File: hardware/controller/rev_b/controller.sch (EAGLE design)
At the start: 96 parts, among them J1 MODULE_CONTROLLER, J14 SOLDERJUMPERTRACE, J15 SOLDERJUMPERTRACE, J2 DM3AT-SF-PEJM5, J3 U.FL-R-SMT, J4 MICRO_USB_B_HIROSE_ZX62-B-5PA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, J5 MICRO_USB_B_HIROSE_ZX62-B-5PA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, J6 TC2030-JLINK-L, J7 TC2030-JLINK-L, J8 JUMPER-3PTH, Q1 MOSFET-NCHANNELSMD, Q2 NX3008PBK, SW1 PTS810SJ, SW2 SIP3240X, U1 SAM4LC8AA, U2 SAM4LC8AA, U3 RXM-GPS-RM-T, U4 FM25CLXXB-DG, U5 TS3USB30E, U6 FTDI234XD, U7 TXS0108EVQFN20, X1 16MHz, X2 16MHz

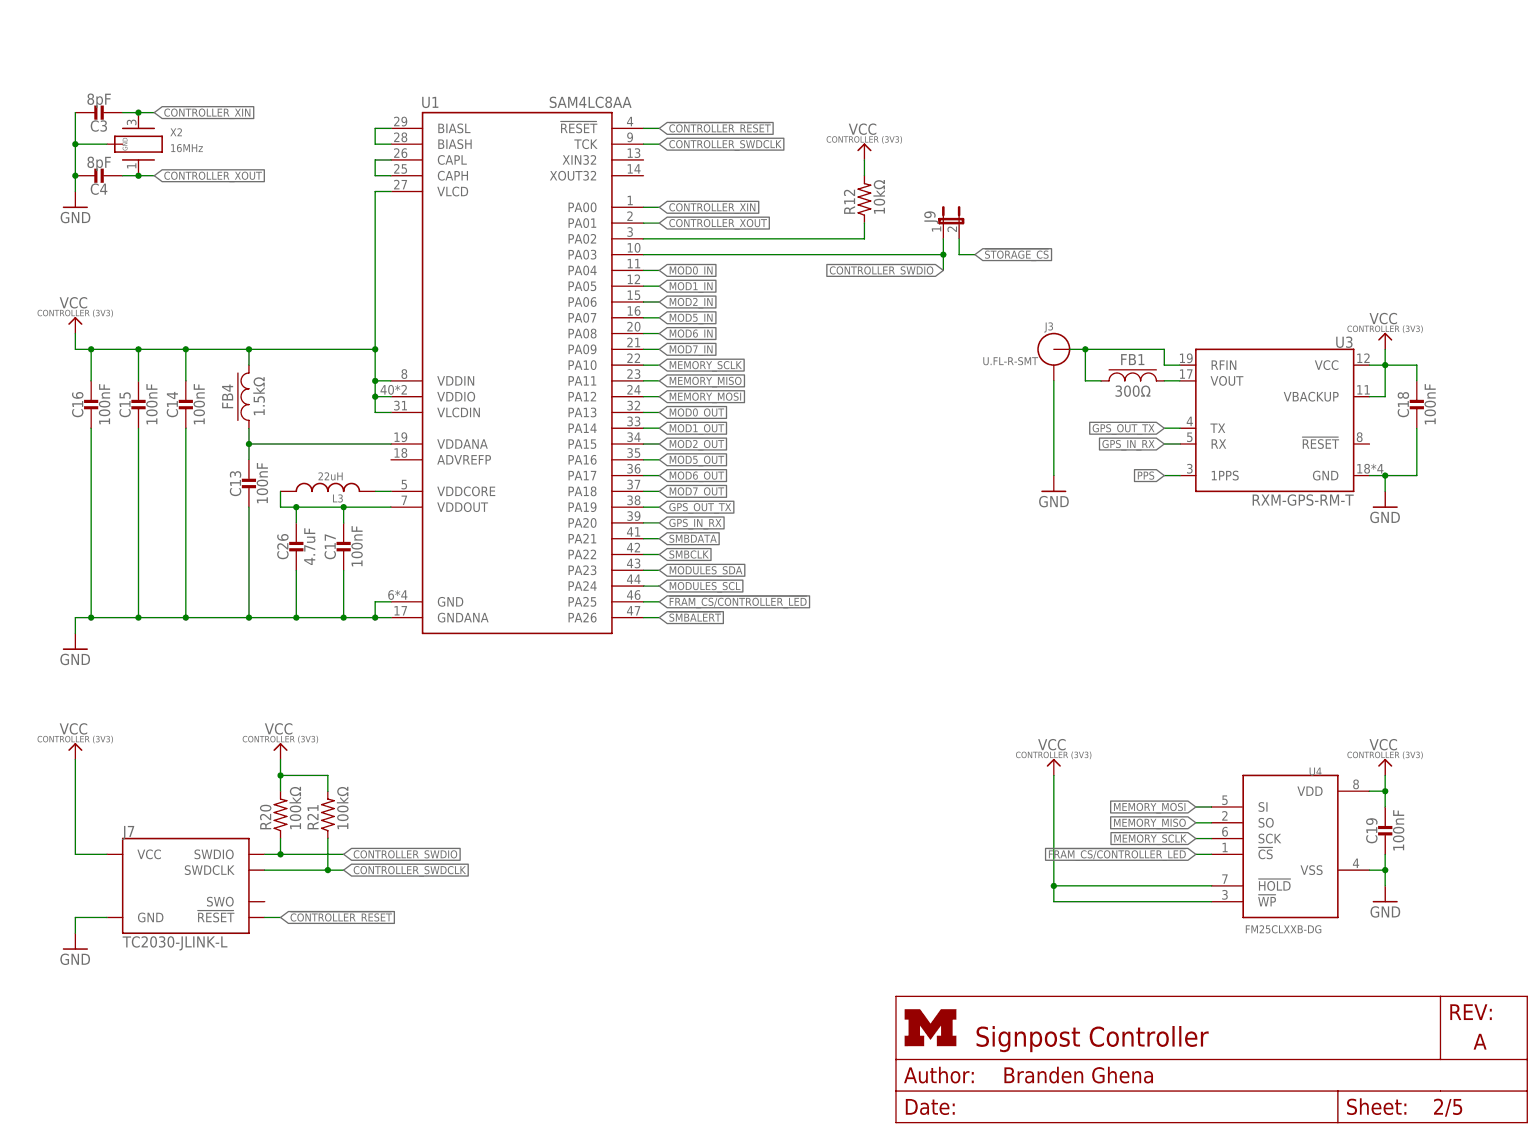
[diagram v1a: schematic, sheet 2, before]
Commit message: Controller rev B, schematic is complete
Updates:
 * Power gates for SD Card and GPS (that should work)
 * Re-do USB OTG circuitry based on [Intel Edison Gateway v3](https://github.com/lab11/IntelEdisonGateway/tree/master/hardware/v3)
 * Add debug headers
 * Upgrade to 64-pin SAM4Ls
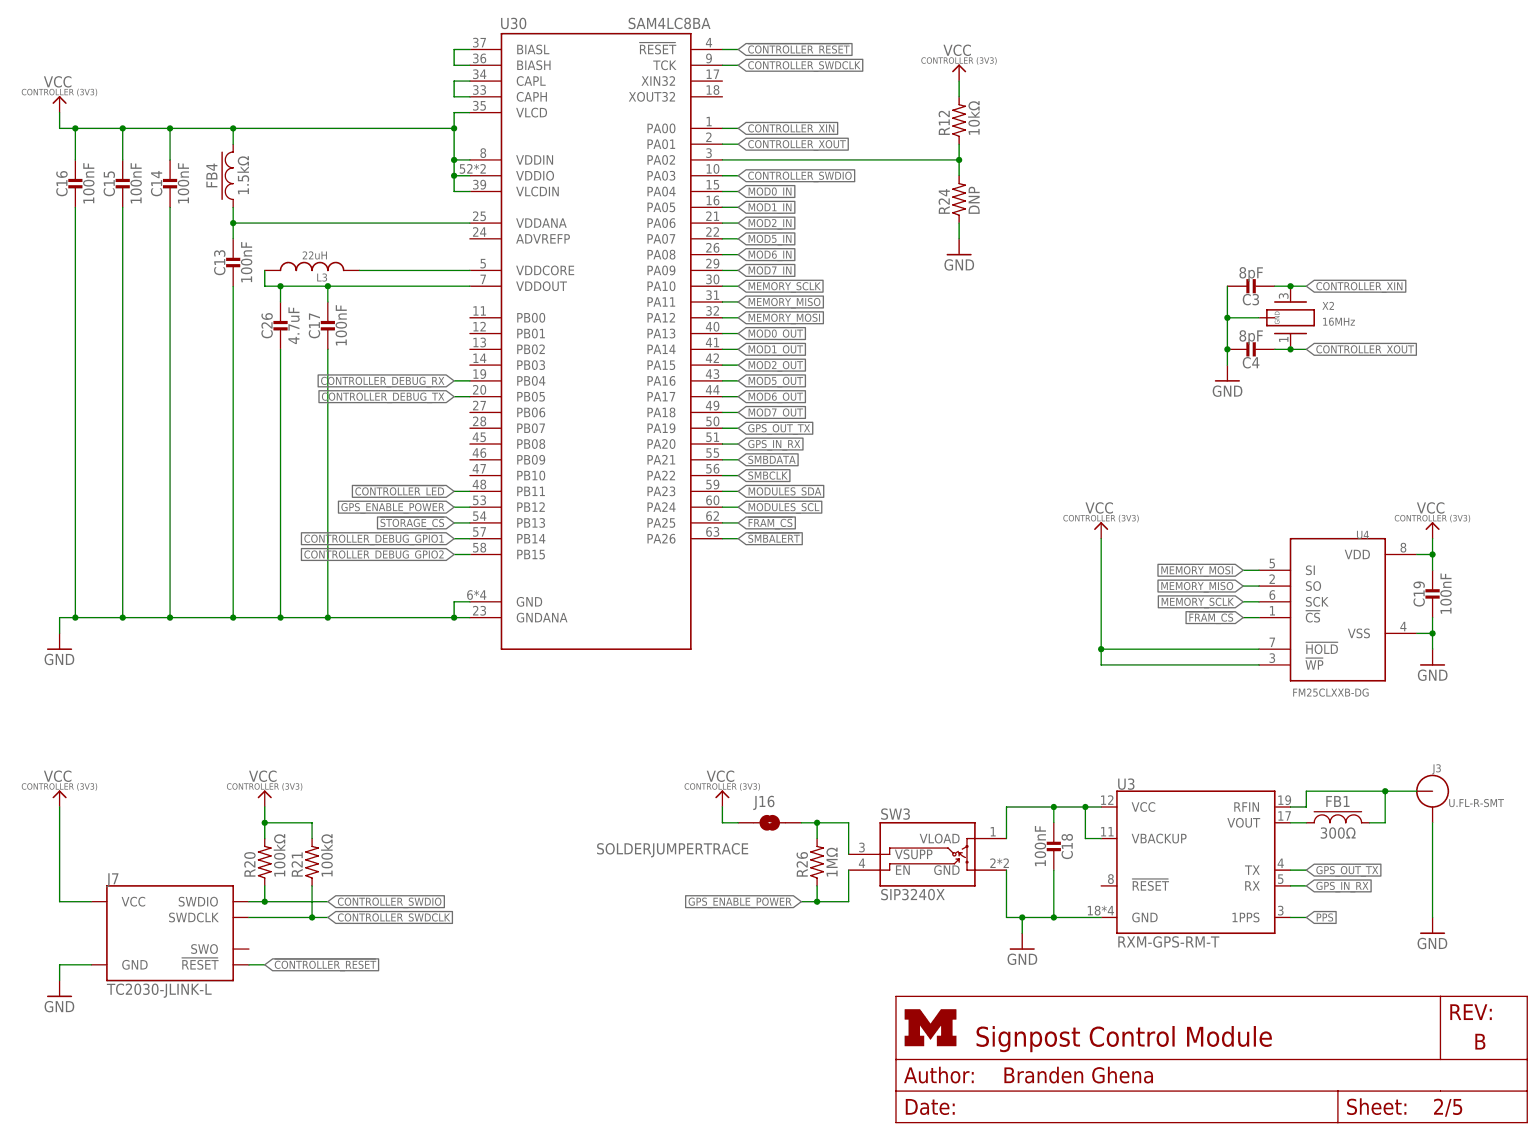
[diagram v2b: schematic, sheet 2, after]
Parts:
- removed J4: MICRO_USB_B_HIROSE_ZX62-B-5PA(11), connector:MICRO_USB_B_HIROSE_ZX62-B-5PA(11)
- removed J8: JUMPER-3PTH, umich:JUMPER-3PTH
- removed J9: (no value), umich:JUMPER-2PTH
- removed Q2: NX3008PBK, fets:NX3008PBK
- removed U1, U2: SAM4LC8AA, chips:SAM4LC8AA
- added J16, J17: SOLDERJUMPERTRACE, SparkFun-Passives:SOLDERJUMPERTRACE
- added J18: MICRO_USB_B_HIROSE_ZX62R-B-5P, connector:MICRO_USB_B_HIROSE_ZX62R-B-5P
- added R26, R27: 1MΩ, passives:RESISTOR0402_RES
- added R28: DNP, passives:RESISTOR0402_RES
- added SW3, SW4: SIP3240X, signpost:SIP3240X
- added U29, U30: SAM4LC8BA, chips:SAM4LC8BA
- added U8: SN74LVC1G125DBVR, chips:SN74LVC1G125DBVR
- J5: value MICRO_USB_B_HIROSE_ZX62-B-5PA(11) -> MICRO_USB_B_HIROSE_ZX62R-B-5P; device connector:MICRO_USB_B_HIROSE_ZX62-B-5PA(11) -> connector:MICRO_USB_B_HIROSE_ZX62R-B-5P; DIGIKEY (none) -> H125274CT-ND
- Q1: value MOSFET-NCHANNELSMD -> DMN32D2LDF; device fets:MOSFET-NCHANNELSMD -> fets:DMN32D2LDF; DIGIKEY SI2312CDS-T1-GE3CT-ND -> (none)
- R13: value 10kΩ -> 100kΩ; DIGIKEY 1276-3431-1-ND -> 1276-3429-1-ND
- R23: value 332kΩ -> 100kΩ; DIGIKEY 1276-4245-1-ND -> 1276-3429-1-ND
- R24: value 665kΩ -> DNP; DIGIKEY 1276-4275-1-ND -> 1276-3431-1-ND
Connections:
- removed net !FRAM_CS/CONTROLLER_LED: J10.9, R10.2, U1.PA25, U4.!CS
- removed net N$16: J8.1, R23.1, R24.2
- removed net N$19: J1CONTROLLER.DBG_TX
- removed net N$20: J1CONTROLLER.DBG_RX
- removed net N$21: J1CONTROLLER.DBG_SWDIO
- removed net N$22: J1CONTROLLER.DBG_SWDCLK
- removed net N$23: J1CONTROLLER.DBG_!RESET
- removed net N$26: J1CONTROLLER.DBG_GPIO1
- removed net N$27: J1CONTROLLER.DBG_GPIO2
- removed net N$33: J1CONTROLLER.GND1
- removed net N$35: J1STORAGE_MASTER.GND1
- removed net N$36: J1STORAGE_MASTER.DBG_GPIO2
- removed net N$39: J1STORAGE_MASTER.DBG_GPIO1
- removed net N$40: J1STORAGE_MASTER.DBG_!RESET
- removed net N$41: J1STORAGE_MASTER.DBG_SWDCLK
- removed net N$42: J1STORAGE_MASTER.DBG_SWDIO
- removed net N$47: J1STORAGE_MASTER.DBG_RX
- removed net N$49: J1STORAGE_MASTER.DBG_TX
- removed net N$52: L3.2, U1.VDDCORE
- removed net SD_DISABLE: Q2.G, R13.2
- removed net SD_ENABLE: U2.PA21
- removed net USB_ATTACHED_3V3: J8.2, Q1.G, U5.S
- new net !CONTROLLER_LED: R10.2, U30.PB11
- new net !FRAM_CS: J10.9, U30.PA25, U4.!CS
- new net CONTROLLER_DEBUG_GPIO1: J1CONTROLLER.DBG_GPIO1, U30.PB14
- new net CONTROLLER_DEBUG_GPIO2: J1CONTROLLER.DBG_GPIO2, U30.PB15
- new net CONTROLLER_DEBUG_RX: J1CONTROLLER.DBG_RX, U30.PB04
- new net CONTROLLER_DEBUG_TX: J1CONTROLLER.DBG_TX, U30.PB05
- new net GPS_ENABLE_POWER: R26.1, SW3.EN, U30.PB12
- new net N$55: J16.2, R26.2, SW3.VSUPP
- new net N$56: C18.1, SW3.VLOAD, U3.VBACKUP, U3.VCC
- new net N$57: J17.2, R27.2, SW4.VSUPP
- new net N$58: C27.1, J2.VCC, R14.2, R15.2, R16.2, R22.2, SW4.VLOAD
- new net N$59: L3.2, U30.VDDCORE
- new net SD_ENABLE_POWER: R27.1, SW4.EN, U29.PA21
- new net STORAGE_DEBUG_GPIO1: J1STORAGE_MASTER.DBG_GPIO1, U29.PB04
- new net STORAGE_DEBUG_GPIO2: J1STORAGE_MASTER.DBG_GPIO2, U29.PB05
- new net STORAGE_DEBUG_RX: J1STORAGE_MASTER.DBG_RX, U29.PB09
- new net STORAGE_DEBUG_TX: J1STORAGE_MASTER.DBG_TX, U29.PB10
- net !CONTROLLER_RESET: now also J1CONTROLLER.DBG_!RESET, U30.!RESET; no longer U1.!RESET
- net !EDISON_PWRBTN: now also U29.PA05; no longer U2.PA05
- net !EDISON_SPI_CS: now also U29.PA22; no longer U2.PA22
- net !SD_CS: now also U29.PA13; no longer U2.PA13
- net !SMBALERT: now also U30.PA26; no longer U1.PA26
- net !STORAGE_CS: now also U29.PA09, U30.PB13; no longer J9.2, U2.PA09
- net !STORAGE_LED: now also U29.PA07; no longer U2.PA07
- net !STORAGE_RESET: now also J1STORAGE_MASTER.DBG_!RESET, U29.!RESET; no longer U2.!RESET
- net CONTROLLER_BUCK/LDO_N: now also R24.2, U30.PA02; no longer U1.PA02
- net CONTROLLER_SWDCLK: now also J1CONTROLLER.DBG_SWDCLK, U30.TCK; no longer U1.TCK
- net CONTROLLER_SWDIO: now also J1CONTROLLER.DBG_SWDIO, U30.PA03; no longer J9.1, U1.PA03
- net CONTROLLER_XIN: now also U30.PA00; no longer U1.PA00
- net CONTROLLER_XOUT: now also U30.PA01; no longer U1.PA01
- net D+: now also J18.D+; no longer J5.D+
- net D-: now also J18.D-; no longer J5.D-
- net EDISON_SPI_MISO: now also U29.PA20; no longer U2.PA20
- net EDISON_SPI_MOSI: now also U29.PA19; no longer U2.PA19
- net EDISON_SPI_SCLK: now also U29.PA18; no longer U2.PA18
- net GND: now also J18.GND, J1CONTROLLER.GND1, J1STORAGE_MASTER.GND1, R13.2, R28.1, SW3.GND, SW4.GND, U29.GND, U29.GNDANA, U30.GND, U30.GNDANA, U8.A, U8.GND; no longer J4.GND, R13.1, U1.GND, U1.GNDANA, U2.GND, U2.GNDANA
- net GPS_IN_RX: now also U30.PA20; no longer U1.PA20
- net GPS_OUT_TX: now also U30.PA19; no longer U1.PA19
- net LINUX_ENABLE_POWER: now also U29.PA06; no longer U2.PA06
- net MEMORY_MISO: now also U29.PA12, U30.PA11; no longer U1.PA11, U2.PA12
- net MEMORY_MOSI: now also U29.PA11, U30.PA12; no longer U1.PA12, U2.PA11
- net MEMORY_SCLK: now also U29.PA10, U30.PA10; no longer U1.PA10, U2.PA10
- net MOD0_IN: now also U30.PA04; no longer U1.PA04
- net MOD0_OUT: now also U30.PA13; no longer U1.PA13
- net MOD1_IN: now also U30.PA05; no longer U1.PA05
- net MOD1_OUT: now also U30.PA14; no longer U1.PA14
- net MOD2_IN: now also U30.PA06; no longer U1.PA06
- net MOD2_OUT: now also U30.PA15; no longer U1.PA15
- net MOD5_IN: now also U30.PA07; no longer U1.PA07
- net MOD5_OUT: now also U30.PA16; no longer U1.PA16
- net MOD6_IN: now also U30.PA08; no longer U1.PA08
- net MOD6_OUT: now also U30.PA17; no longer U1.PA17
- net MOD7_IN: now also U30.PA09; no longer U1.PA09
- net MOD7_OUT: now also U30.PA18; no longer U1.PA18
- net MODULES_SCL: now also U29.PA24, U30.PA24; no longer U1.PA24, U2.PA24
- net MODULES_SDA: now also U29.PA23, U30.PA23; no longer U1.PA23, U2.PA23
- net N$10: now also J18.+5V; no longer J5.+5V
- net N$17: now also E_1_USB.USB_ID, U8.Y; no longer C27.1, J2.VCC, Q2.D, R14.2, R15.2, R16.2, R22.2
- net N$29: now also U29.VDDANA; no longer U2.VDDANA
- net N$30: now also Q1.D2, R23.2, U5.S; no longer E_1_USB.USB_ID, Q1.D
- net N$32: now also U30.VDDANA; no longer U1.VDDANA
- net N$44: now also U30.VDDOUT; no longer U1.VDDOUT
- net N$45: now also U29.VDDOUT; no longer U2.VDDOUT
- net N$46: now also U29.VDDCORE; no longer U2.VDDCORE
- net N$48: now also U29.CAPH, U29.CAPL; no longer U2.CAPH, U2.CAPL
- net N$5: now also J5.D-, U5.D1-; no longer J4.D-, U5.D2-
- net N$51: now also U29.BIASH, U29.BIASL; no longer U2.BIASH, U2.BIASL
- net N$53: now also U30.BIASH, U30.BIASL; no longer U1.BIASH, U1.BIASL
- net N$54: now also U30.CAPH, U30.CAPL; no longer U1.CAPH, U1.CAPL
- net N$6: now also J5.D+, U5.D1+; no longer J4.D+, U5.D2+
- net N$7: now also D2.R; no longer D2.B
- net N$9: now also D2.B; no longer D2.R
- net SD_DETECT: now also U29.PA17; no longer U2.PA17
- net SD_MISO: now also U29.PA15; no longer U2.PA15
- net SD_MOSI: now also U29.PA16; no longer U2.PA16
- net SD_SCLK: now also U29.PA14; no longer U2.PA14
- net SMBCLK: now also U30.PA22; no longer U1.PA22
- net SMBDATA: now also U30.PA21; no longer U1.PA21
- net STORAGE_BUCK/LDO_N: now also R28.2, U29.PA02; no longer U2.PA02
- net STORAGE_SWDCLK: now also J1STORAGE_MASTER.DBG_SWDCLK, U29.TCK; no longer U2.TCK
- net STORAGE_SWDIO: now also J1STORAGE_MASTER.DBG_SWDIO, U29.PA03; no longer U2.PA03
- net STORAGE_XIN: now also U29.PA00; no longer U2.PA00
- net STORAGE_XOUT: now also U29.PA01; no longer U2.PA01
- net USB_MOD_D+: now also U5.D2+; no longer U5.D1+
- net USB_MOD_D-: now also U5.D2-; no longer U5.D1-
- net USB_VBUS: now also J5.+5V, Q1.G2, R13.1, U8.!OE; no longer J4.+5V, R23.2
- net VCC_CONTROLLER: now also J16.1, J17.1, U29.VDDIN, U29.VDDIO, U29.VLCD, U29.VLCDIN, U30.VDDIN, U30.VDDIO, U30.VLCD, U30.VLCDIN; no longer C18.1, Q2.S, U1.VDDIN, U1.VDDIO, U1.VLCD, U1.VLCDIN, U2.VDDIN, U2.VDDIO, U2.VLCD, U2.VLCDIN, U3.VBACKUP, U3.VCC
- net VCC_LINUX: now also U8.VCC
- net VCC_LINUX_3V3: now also R23.1; no longer J8.3
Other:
- note added: "Automatically switch to OTG peripheral when programming USB is attached"
- note added: "Power gate"
- note added: "SAM4L Oscillator"
- note added: "Top mount"
- note removed: "Bottom mount"
- moved on the sheet: C1, C10, C11, C12, C13, C14, C15, C16, C17, C18, C19, C2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

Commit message: Working through routing
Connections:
- removed net N$55: J16.2, R26.2, SW3.VSUPP
- removed net N$57: J17.2, R27.2, SW4.VSUPP
- new net N$16: J14.1, SW2.VLOAD
- new net N$19: J16.1, SW3.VLOAD
- net LINUX_5V_IN: now also J14.2; no longer SW2.VLOAD
- net N$18: now also J17.1, SW4.VLOAD; no longer J14.2, R25.2, SW2.VSUPP
- net N$56: now also J16.2; no longer SW3.VLOAD
- net N$58: now also J17.2; no longer SW4.VLOAD
- net VCC_CONTROLLER: now also R26.2, R27.2, SW3.VSUPP, SW4.VSUPP; no longer J16.1, J17.1
- net VCC_LINUX: now also R25.2, SW2.VSUPP; no longer J14.1
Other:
- moved on the sheet: J14, J16, J17, R25, R26, SW2, SW3

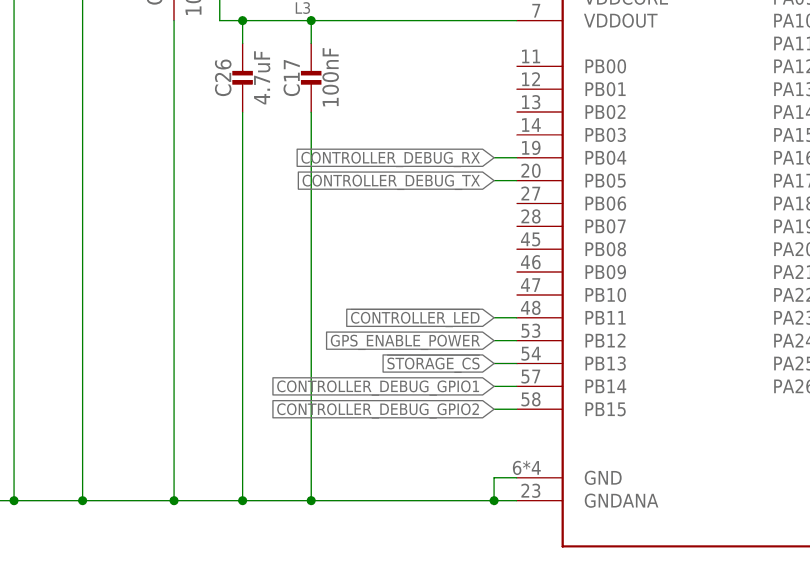
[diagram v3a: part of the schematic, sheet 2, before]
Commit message: Everything but the debug. 39 airwires to go
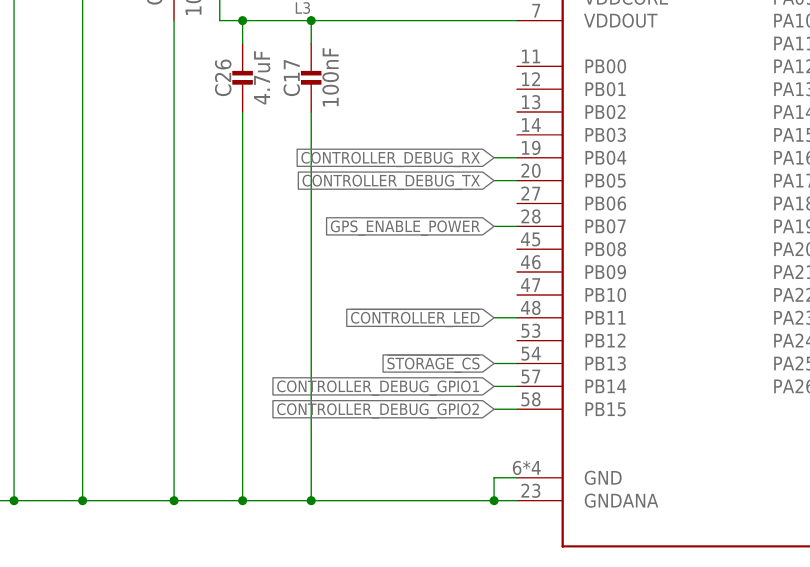
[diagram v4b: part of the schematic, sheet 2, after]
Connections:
- net GPS_ENABLE_POWER: now also U30.PB07; no longer U30.PB12
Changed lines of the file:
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@@
 </segment>
 <segment>
-<pinref part="U30" gate="U1" pin="PB12"/>
-<wire x1="78.74" y1="99.06" x2="76.2" y2="99.06" width="0.1524" layer="91"/>
-<label x="76.2" y="99.06" size="1.27" layer="95" font="vector" rot="R180" xref="yes"/>
+<pinref part="U30" gate="U1" pin="PB07"/>
+<wire x1="78.74" y1="111.76" x2="76.2" y2="111.76" width="0.1524" layer="91"/>
+<label x="76.2" y="111.76" size="1.27" layer="95" font="vector" rot="R180" xref="yes"/>
 </segment>
 </net>

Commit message: Checkpoint. 30 airwires
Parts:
- added J472: (no value), pinhead:PINHD-2X3
- added S1: B3U-1000P, switches:B3U-1000P
- D4: DIGIKEY P18981CT-ND -> 478-7800-1-ND
- renumbered D1 to D4
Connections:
- removed net N$31: E_1_GPIO.GP182_PWM2, U7.A7
- removed net N$43: E_1_GPIO.GP12_PWM0, U7.A8
- new net EDISON_LED1: E_1_GPIO.GP182_PWM2, J472.4, U7.A7
- new net EDISON_LED2: E_1_GPIO.GP12_PWM0, J472.3, U7.A8
- net !EDISON_PWRBTN: now also J472.2, S1.P$1
- net EDISON_UART_RX: now also J472.6
- net EDISON_UART_TX: now also J472.5
- net GND: now also J472.1, S1.P$2
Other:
- note added: "Main Decoupling Capacitor"
- moved on the sheet: C29, J10, J11, J12

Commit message: Routing complete!!
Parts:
- FB4: DIGIKEY 490-5216-1-ND -> 1276-6395-1-ND
- L2: DIGIKEY (none) -> 1276-6395-1-ND
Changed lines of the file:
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@@
 <attribute name="DIGIKEY" value="490-5216-1-ND"/>
 </part>
-<part name="L2" library="signpost" deviceset="LHQ3NP" device="" value="22uH"/>
+<part name="L2" library="signpost" deviceset="LHQ3NP" device="" value="22uH">
+<attribute name="DIGIKEY" value="1276-6395-1-ND"/>
+</part>
 <part name="C12" library="passives" deviceset="CAPACITOR" device="0402_CAP" value="100nF">
 <attribute name="DIGIKEY" value="490-10777-1-ND"/>
@@
 </part>
 <part name="FB4" library="passives" deviceset="FERRITE_BEAD" device="0402" value="1.5kΩ">
-<attribute name="DIGIKEY" value="490-5216-1-ND"/>
+<attribute name="DIGIKEY" value="1276-6395-1-ND"/>
 </part>
 <part name="L3" library="signpost" deviceset="LHQ3NP" device="" value="22uH"/>
